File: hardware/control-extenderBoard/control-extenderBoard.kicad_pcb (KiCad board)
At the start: 4 copper layers, 197.5 x 108.9 mm, 171 parts, among them J1 12V + GND (TP), J10 SCL6 + GND (TP), J11 SDA6 + GND (TP), J12 3V3 + GND (TP), J13 12V + GND (TP), J14 SCL6 + GND (TP), J15 SDA6 + GND (TP), J16 12V + GND (TP), J17 24V IN, J18 GND, J19 3V3 + GND (TP), J20 SCL6 + GND (TP), J21 SDA6 + GND (TP), J22 SDA, SCL - ESP32, J23 I2C Reserve SCL/GND, J24 I2C Reserve SDA/GND, J25 I2C Reserve SDA/GND, J26 I2C Reserve SCL/GND, J27 CAT6-Shield, J28 CAT6-Shield, J29 Chassis, J3 Conn_01x02_Pin, J30 RX TX, J31 DIR, GND, J32 12V out, J33 5V out, J34 3V3 out, J35 Conn_01x02_Pin, J36 Conn_01x02_Pin, J37 Conn_01x02_Pin, J38 Conn_01x02_Pin, J39 Conn_01x02_Pin, J4 3V3 + GND (TP), J5 GND, J6 SCL7 Differential (TP), J7 SDA7 Differential (TP), J8 RS485, J9 Conn_01x03_Pin, U1 MAX3485, U10 LM2576T-12, U13 AS5600_Breakout, U14 PCA9600D, U2 PCA9600D, U3 TCA9548A_1-to-8_I2C_Multiplex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, U4 LM2576T-3.3, U5 PCA9600D, U6 PCA82C251, U7 PCA82C251, U8 PCA9600D, U9 LM2576T-5

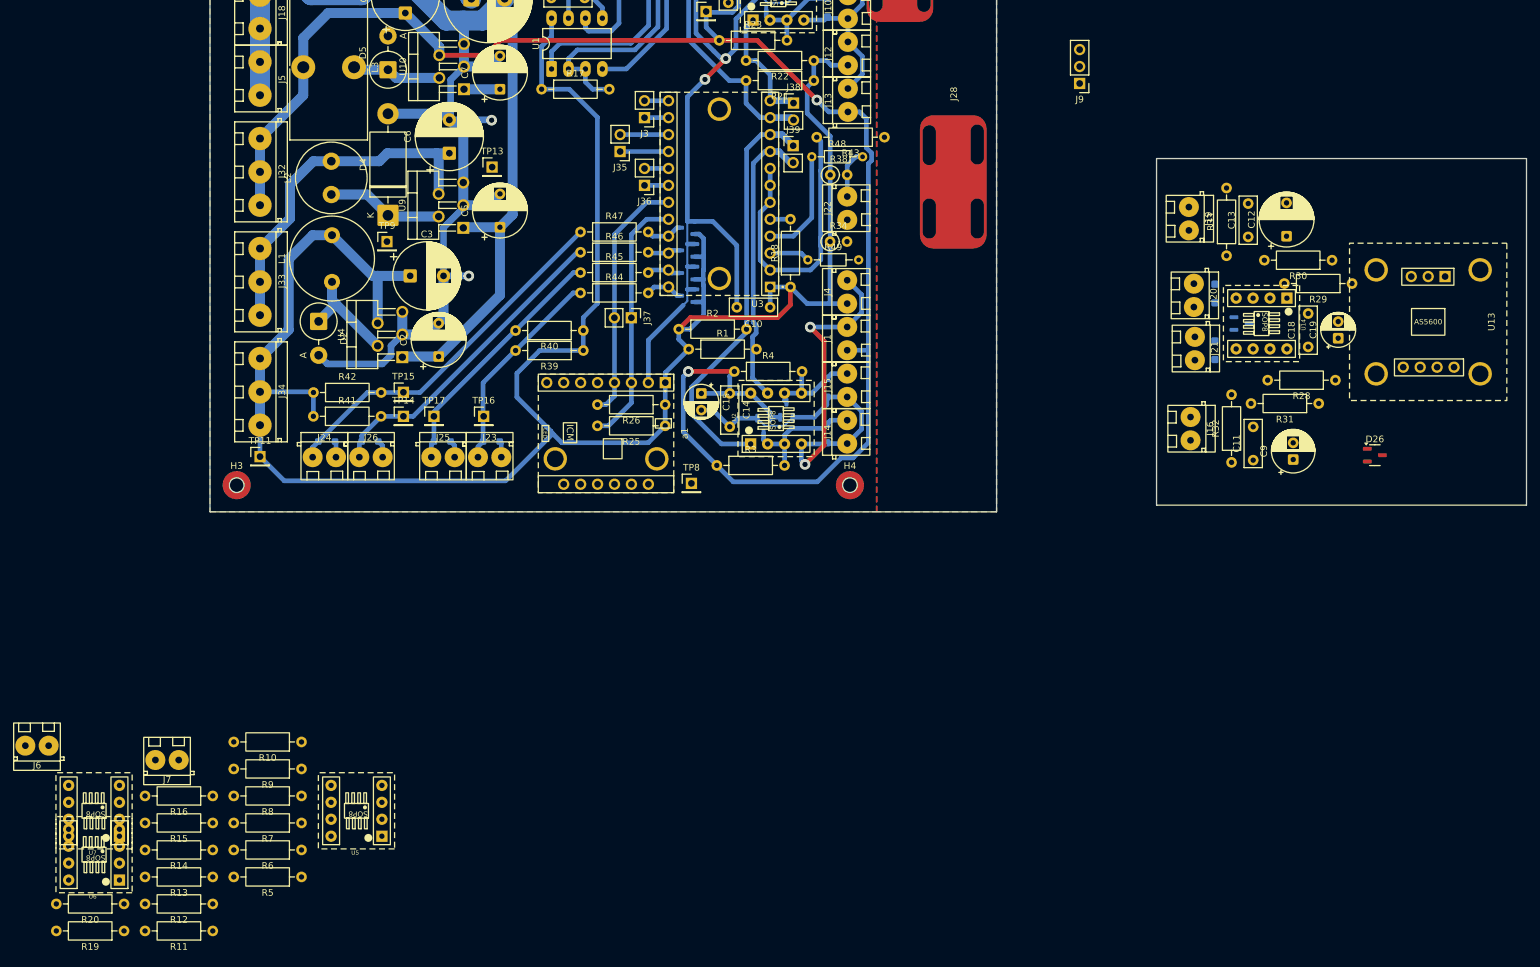
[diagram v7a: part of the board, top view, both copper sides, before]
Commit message: extenderBoard: Add pcb text, Arrange remote-board
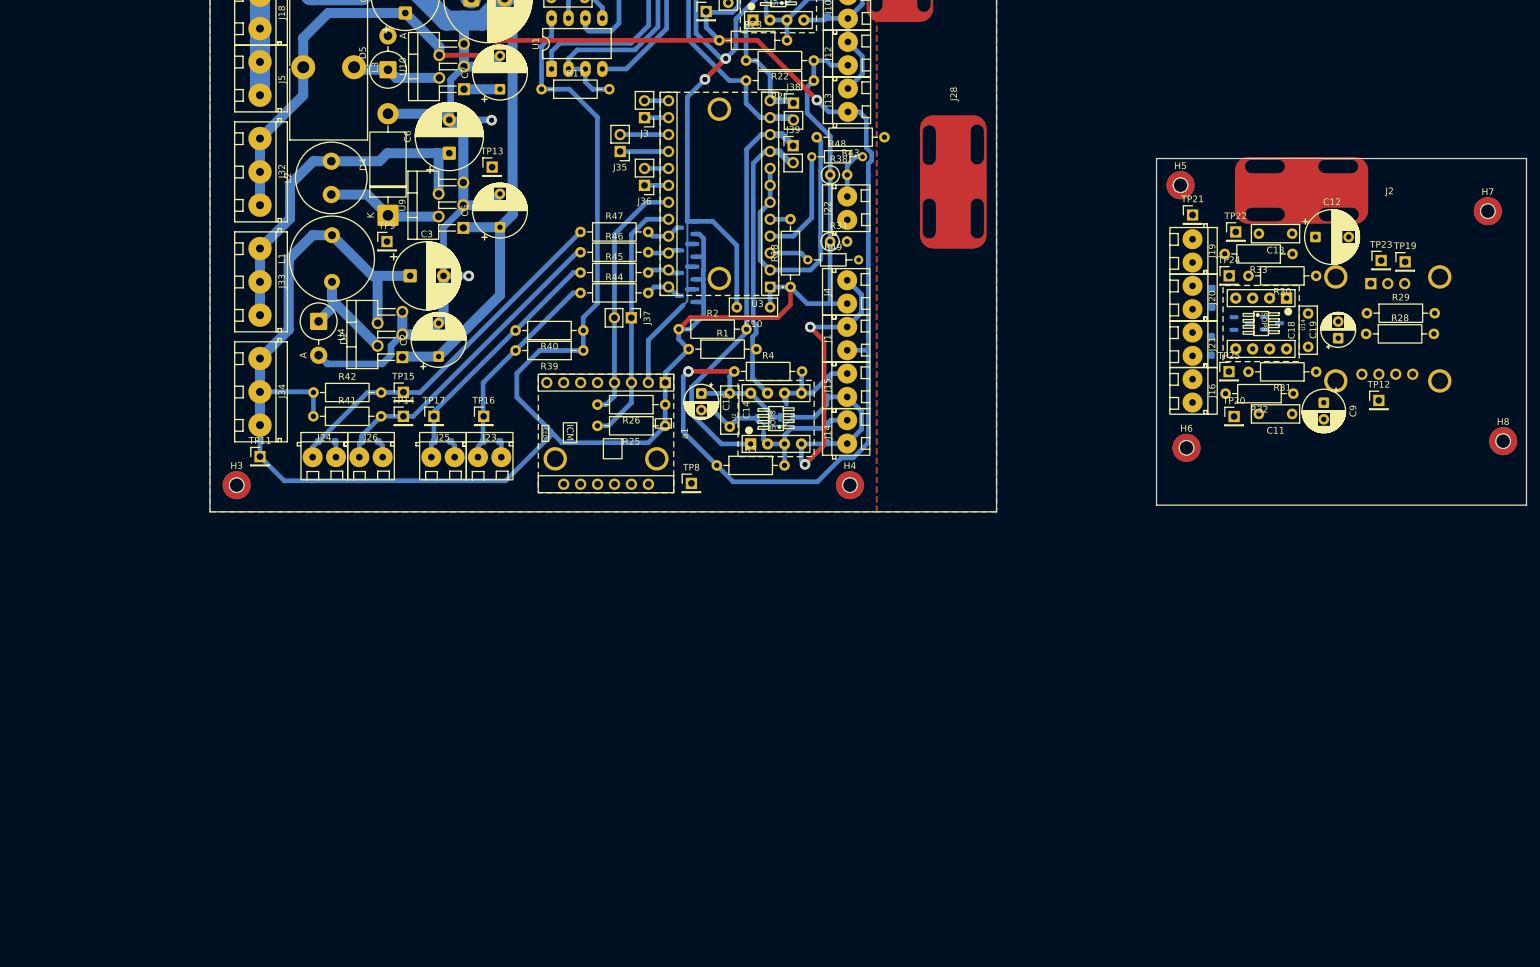
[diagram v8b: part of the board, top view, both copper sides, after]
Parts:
- removed J6: SCL7 Differential (TP), terminals_libJonny:ScrewTerminal_P3.5mm_2Pin_FP7x7
- removed J7: SDA7 Differential (TP), terminals_libJonny:ScrewTerminal_P3.5mm_2Pin_FP7x7
- removed J9: Conn_01x03_Pin, Connector_PinHeader_2.54mm:PinHeader_1x03_P2.54mm_Vertical
- removed R10, R12, R7, R9: 390, Resistor_THT:R_Axial_DIN0207_L6.3mm_D2.5mm_P10.16mm_Horizontal
- removed R11, R8: 100, Resistor_THT:R_Axial_DIN0207_L6.3mm_D2.5mm_P10.16mm_Horizontal
- removed R13, R14, R15, R16: 4k7, Resistor_THT:R_Axial_DIN0207_L6.3mm_D2.5mm_P10.16mm_Horizontal
- removed R19, R20: 2k2, Resistor_THT:R_Axial_DIN0207_L6.3mm_D2.5mm_P10.16mm_Horizontal
- removed R5, R6: 1k, Resistor_THT:R_Axial_DIN0207_L6.3mm_D2.5mm_P10.16mm_Horizontal
- removed U5: PCA9600D, modules_libJonny:Adapter-Board_SOP8_to_DIP8
- removed U6, U7: PCA82C251, modules_libJonny:Adapter-Board_SOP8_to_DIP8
- added H5: MountingHole_Pad, mountingHoles_libJonny:MountingHole_2.2mm_NPTH-with-pad_DRC-clearance-error, F.Cu at (190.6, 81.0)
- added H6: MountingHole_Pad, mountingHoles_libJonny:MountingHole_2.2mm_NPTH-with-pad_DRC-clearance-error, F.Cu at (191.5, 120.4)
- added H7: MountingHole_Pad, mountingHoles_libJonny:MountingHole_2.2mm_NPTH-with-pad_DRC-clearance-error, F.Cu at (236.7, 84.9)
- added H8: MountingHole_Pad, mountingHoles_libJonny:MountingHole_2.2mm_NPTH-with-pad_DRC-clearance-error, F.Cu at (239.0, 119.4)
- added J2: CAT6-Shield, misc_libJonny:Shield_Landing_Pad_6mmCable_ZipTie, F.Cu at (208.8, 81.8)
- added TP12: GND, Connector_PinHeader_2.54mm:PinHeader_1x01_P2.54mm_Vertical, F.Cu at (220.3, 113.3)
- added TP19: SCL, Connector_PinHeader_2.54mm:PinHeader_1x01_P2.54mm_Vertical, F.Cu at (224.3, 92.5)
- added TP20: 12V-Filtered, Connector_PinHeader_2.54mm:PinHeader_1x01_P2.54mm_Vertical, F.Cu at (198.6, 115.7)
- added TP21: 3V3-IN, Connector_PinHeader_2.54mm:PinHeader_1x01_P2.54mm_Vertical, F.Cu at (192.4, 85.5)
- added TP22: 3V3-Filtered, Connector_PinHeader_2.54mm:PinHeader_1x01_P2.54mm_Vertical, F.Cu at (198.9, 88.0)
- added TP23: SDA, Connector_PinHeader_2.54mm:PinHeader_1x01_P2.54mm_Vertical, F.Cu at (220.7, 92.3)
- added TP24: SCL-in, Connector_PinHeader_2.54mm:PinHeader_1x01_P2.54mm_Vertical, F.Cu at (197.9, 94.6)
- added TP25: SDA-in, Connector_PinHeader_2.54mm:PinHeader_1x01_P2.54mm_Vertical, F.Cu at (197.9, 109.0)
- D26, U13: moved to B.Cu
- J10: value SCL6 + GND (TP) -> SCL1 + GND (TP)
- J11: value SDA6 + GND (TP) -> SDA1 + GND (TP)
- J23: value I2C Reserve SCL/GND -> I2C7 Reserve SCL/GND
- J24: value I2C Reserve SDA/GND -> I2C6 Reserve SDA/GND
- J25: value I2C Reserve SDA/GND -> I2C7 Reserve SDA/GND
- J26: value I2C Reserve SCL/GND -> I2C6 Reserve SCL/GND
- J30: value RX TX -> RX DIR
- J31: value DIR, GND -> TX, GND
- TP16: value SCL6 -> SCL7
- TP17: value SDA6 -> SDA7
- moved D26 25.1 mm to (204.3, 101.7)
- moved R32 13.9 mm to (207.5, 112.3), turned to 180 degrees
- moved R33 9.89 mm to (207.4, 91.3), turned to 180 degrees
- moved C9 9.68 mm to (212.1, 113.6), turned to -90 degrees
- moved C11 9.07 mm to (207.4, 115.3), turned to 180 degrees
- moved R28 8.34 mm to (218.4, 103.3), turned to 0 degrees
- moved D16 7.87 mm to (195.2, 105.1)
- moved D15 7.86 mm to (195.3, 97.9)
- moved C13 6.62 mm to (207.4, 88.3), turned to 180 degrees
- moved U13 6.15 mm to (221.7, 102.6)
- moved J16 5.68 mm to (192.4, 110.1)
- moved R29 4.98 mm to (218.6, 100.2), turned to 0 degrees
- moved J19 4.86 mm to (192.4, 89.1)
- moved R31 4.77 mm to (210.9, 109.0)
- moved C12 4.33 mm to (210.8, 88.8), turned to 0 degrees
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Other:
- board text added: "12V"
- board text added: "12V 1.5A"
- board text added: "24V"
- board text added: "3V3"
- board text added: "3V3 2A"
- board text added: "5V"
- board text added: "5V 1A"
- board text added: "BATT"
- board text added: "DE"
- board text added: "GND"
- board text added: "Gyroscope ICM42688"
- board text added: "I2C MUX TCA9548A"
- board text added: "MASTER"
- board text added: "R+"
- board text added: "R-"
- board text added: "RX"
- board text added: "SCL0"
- board text added: "SCL2"
- board text added: "SCL3"
- board text added: "SCL4"
- board text added: "SCL5"
- board text added: "SCL6"
- board text added: "SCL7"
- board text added: "SDA SCL"
- board text added: "SDA0"
- board text added: "SDA1"
- board text added: "SDA2"
- board text added: "SDA3"
- board text added: "SDA4"
- board text added: "SDA5"
- board text added: "SDA6"
- board text added: "SDA7"
- board text added: "Shield"
- board text added: "TX"
